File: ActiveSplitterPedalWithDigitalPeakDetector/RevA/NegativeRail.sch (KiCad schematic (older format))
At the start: 5 parts, among them U3 TPS60400

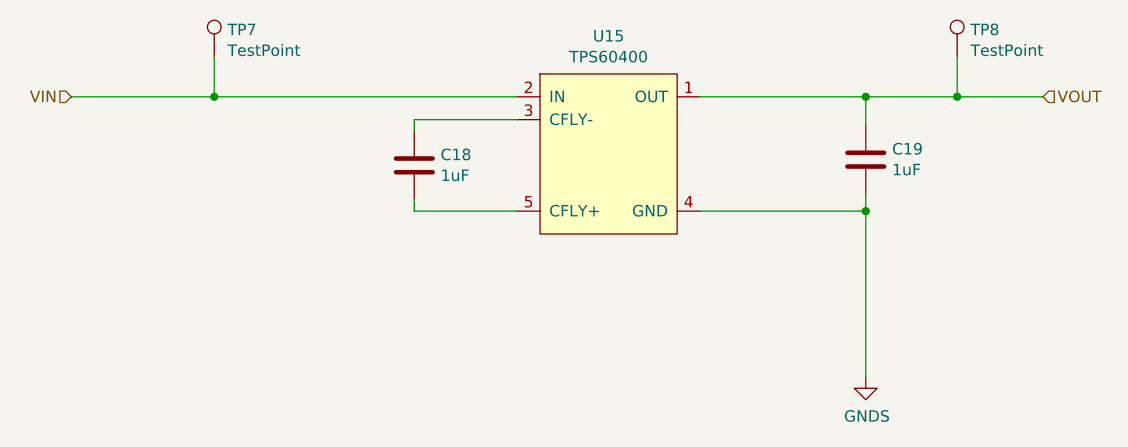
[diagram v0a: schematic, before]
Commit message: hw update
moved led resistors to back copper layer
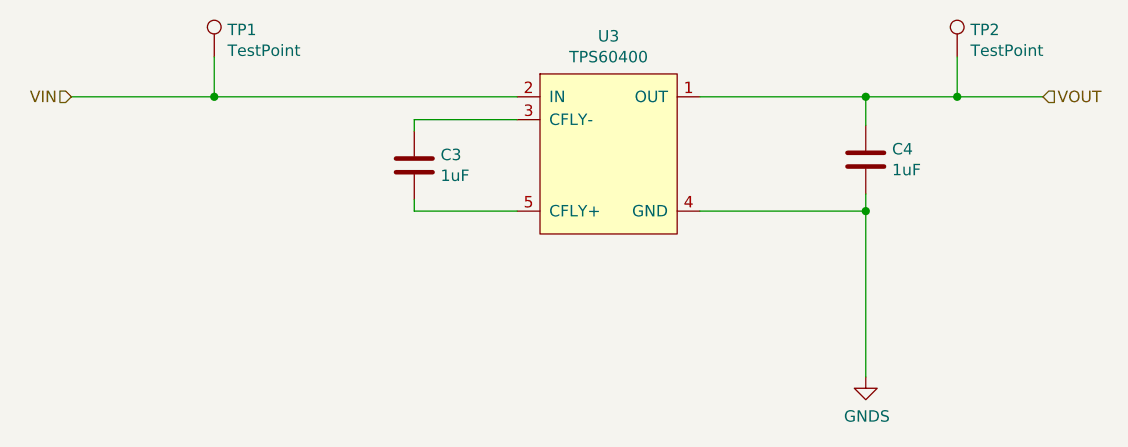
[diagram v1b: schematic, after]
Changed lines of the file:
@@
 $Descr A4 11693 8268
 encoding utf-8
-Sheet 12 15
+Sheet 6 15
 Title ""
 Date ""
@@
 AR Path="/5F6F456E/5F6CB881" Ref="U14"  Part="1"
 AR Path="/5F6F8B66/5F6CB881" Ref="U15"  Part="1"
-F 0 "U15" H 5300 3915 50  0000 C CNN
+F 0 "U3" H 5300 3915 50  0000 C CNN
 F 1 "TPS60400" H 5300 3824 50  0000 C CNN
 F 2 "Package_TO_SOT_SMD:SOT-23-5_HandSoldering" H 5300 3823 50  0001 C CNN
@@
 AR Path="/5F6F456E/5F6CBB44" Ref="C7"  Part="1"
 AR Path="/5F6F8B66/5F6CBB44" Ref="C18"  Part="1"
-F 0 "C18" H 4565 3496 50  0000 L CNN
+F 0 "C3" H 4565 3496 50  0000 L CNN
 F 1 "1uF" H 4565 3405 50  0000 L CNN
 F 2 "Capacitor_SMD:C_0805_2012Metric_Pad1.15x1.40mm_HandSolder" H 4488 3300 50  0001 C CNN
@@
 AR Path="/5F6F456E/5F6CC1BA" Ref="#PWR0150"  Part="1"
 AR Path="/5F6F8B66/5F6CC1BA" Ref="#PWR0157"  Part="1"
-F 0 "#PWR0157" H 6425 4125 50  0001 C CNN
+F 0 "#PWR0110" H 6425 4125 50  0001 C CNN
 F 1 "GNDS" H 6430 4202 50  0000 C CNN
 F 2 "" H 6425 4375 50  0001 C CNN
@@
 AR Path="/5F6F456E/5F6CC20E" Ref="C11"  Part="1"
 AR Path="/5F6F8B66/5F6CC20E" Ref="C19"  Part="1"
-F 0 "C19" H 6540 3471 50  0000 L CNN
+F 0 "C4" H 6540 3471 50  0000 L CNN
 F 1 "1uF" H 6540 3380 50  0000 L CNN
 F 2 "Capacitor_SMD:C_0805_2012Metric_Pad1.15x1.40mm_HandSolder" H 6463 3275 50  0001 C CNN
@@
 AR Path="/5F6F456E/5F6DE647" Ref="TP5"  Part="1"
 AR Path="/5F6F8B66/5F6DE647" Ref="TP7"  Part="1"
-F 0 "TP7" H 3633 3093 50  0000 L CNN
+F 0 "TP1" H 3633 3093 50  0000 L CNN
 F 1 "TestPoint" H 3633 3002 50  0000 L CNN
 F 2 "TestPoint:TestPoint_Pad_D1.0mm" H 3775 2975 50  0001 C CNN
@@
 AR Path="/5F6F456E/5F6DF27F" Ref="TP6"  Part="1"
 AR Path="/5F6F8B66/5F6DF27F" Ref="TP8"  Part="1"
-F 0 "TP8" H 6883 3093 50  0000 L CNN
+F 0 "TP2" H 6883 3093 50  0000 L CNN
 F 1 "TestPoint" H 6883 3002 50  0000 L CNN
 F 2 "TestPoint:TestPoint_Pad_D1.0mm" H 7025 2975 50  0001 C CNN
